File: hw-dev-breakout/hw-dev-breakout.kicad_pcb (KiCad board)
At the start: 4 copper layers, 176 parts, among them J101 CN7, J102 CN10, J201 WAGO 250-220, J202 Conn_01x16, J301 WAGO 250-220, J302 Conn_01x20, Q301 2N7002, Q302 2N7002, Q303 2N7002, Q304 2N7002, Q305 2N7002, Q306 2N7002, Q307 2N7002, Q308 HL 20N04, Q309 HL 20N04, Q310 2N7002, Q311 Q_PMOS_HL_4485, SW101 SW_Push, U101 TCAN332, U102 TCAN332, U103 TCAN332, U201 CM1293A-04SO, U202 CM1293A-04SO, U203 CM1293A-04SO, U204 CM1293A-04SO

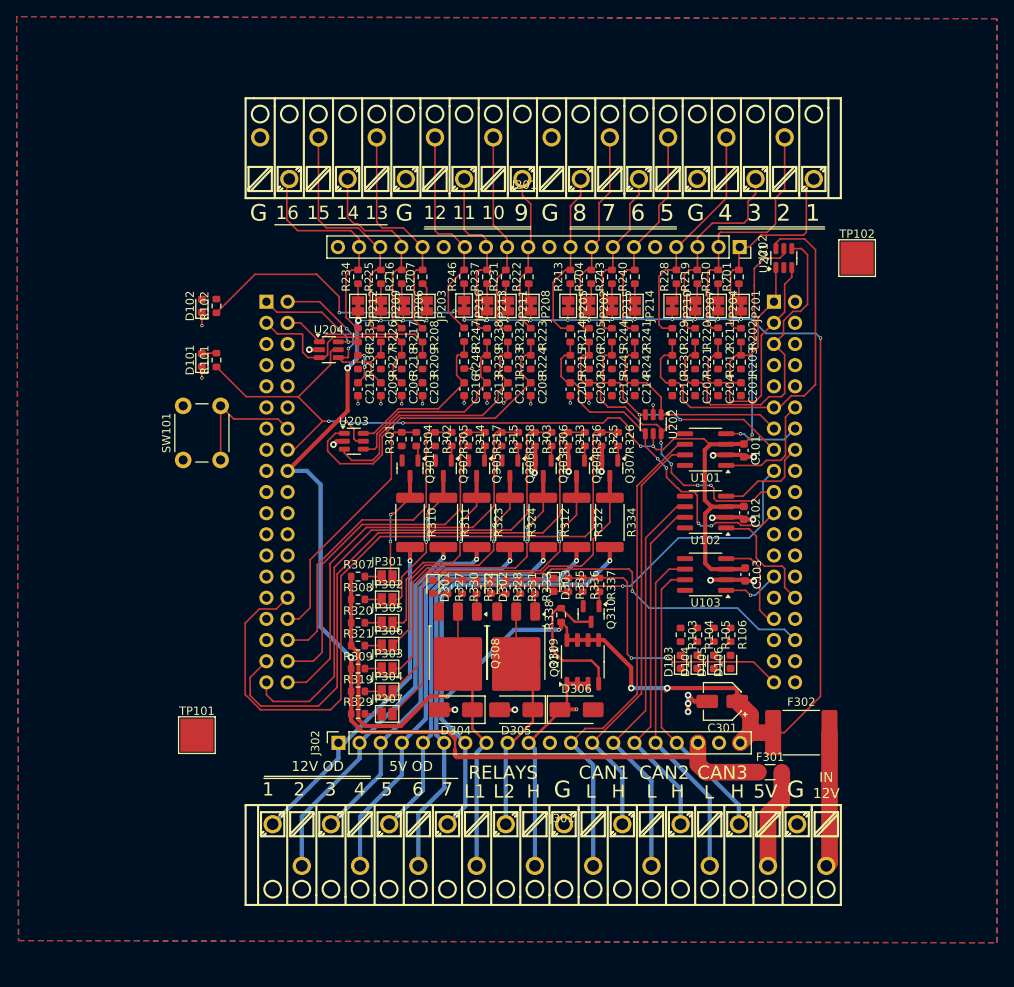
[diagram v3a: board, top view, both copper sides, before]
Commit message: pcb: Routed, using jlc 4 layer specs
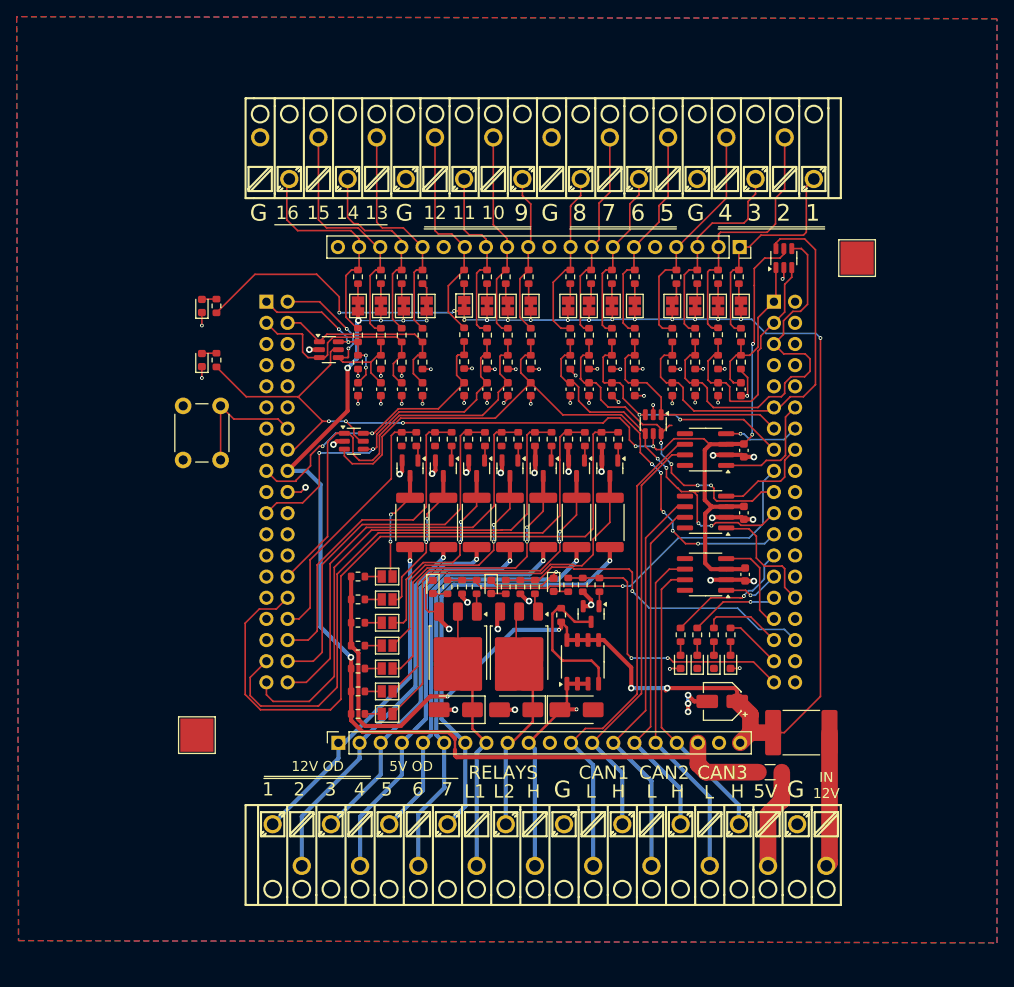
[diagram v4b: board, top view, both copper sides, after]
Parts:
- moved Q309 0.35 mm to (135.1, 104.5)
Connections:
- J102 pad 18: /LED4 -> unconnected-(J102-Pin_18-Pad18)
- J102 pad 2: /LED1 -> unconnected-(J102-Pin_2-Pad2)
- J102 pad 25: unconnected-(J102-Pin_25-Pad25) -> /LED1
- J102 pad 29: unconnected-(J102-Pin_29-Pad29) -> /LED2
- J102 pad 33: unconnected-(J102-Pin_33-Pad33) -> /LED3
- J102 pad 35: unconnected-(J102-Pin_35-Pad35) -> /LED4
- J102 pad 4: /LED2 -> unconnected-(J102-Pin_4-Pad4)
- J102 pad 6: /LED3 -> unconnected-(J102-Pin_6-Pad6)
- U203 pad 1: /IN9 -> /IN10
- U203 pad 3: /IN10 -> /IN9
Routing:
- net GND: track 50.4 -> 110.7 mm, vias 30 -> 64
- net /IN9: track 40.2 -> 77.4 mm, vias 0 -> 5
- net /IN10: track 32.4 -> 54.6 mm
- net /IN11: track 25.3 -> 43.6 mm, vias 0 -> 2
- net /IN12: track 20.8 -> 37.2 mm, vias 0 -> 2
- net /LED1: track 0.00 -> 15.9 mm, vias 0 -> 1
- net /LED2: track 0.00 -> 10.7 mm, vias 0 -> 1
- net /LED3: track 0.00 -> 9.51 mm
- net /LED4: track 0.00 -> 6.86 mm
- net /IN3: track 41.6 -> 46.9 mm
- net /IN13: track 19.5 -> 24.1 mm
- net Net-(D102-A): track 0.00 -> 1.77 mm
- net Net-(D106-A): track 0.00 -> 1.64 mm
- net Net-(D105-A): track 0.00 -> 1.64 mm
- net Net-(D104-A): track 0.00 -> 1.64 mm
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
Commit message: pcb: Routed for 2 layer, fixed P-fet error
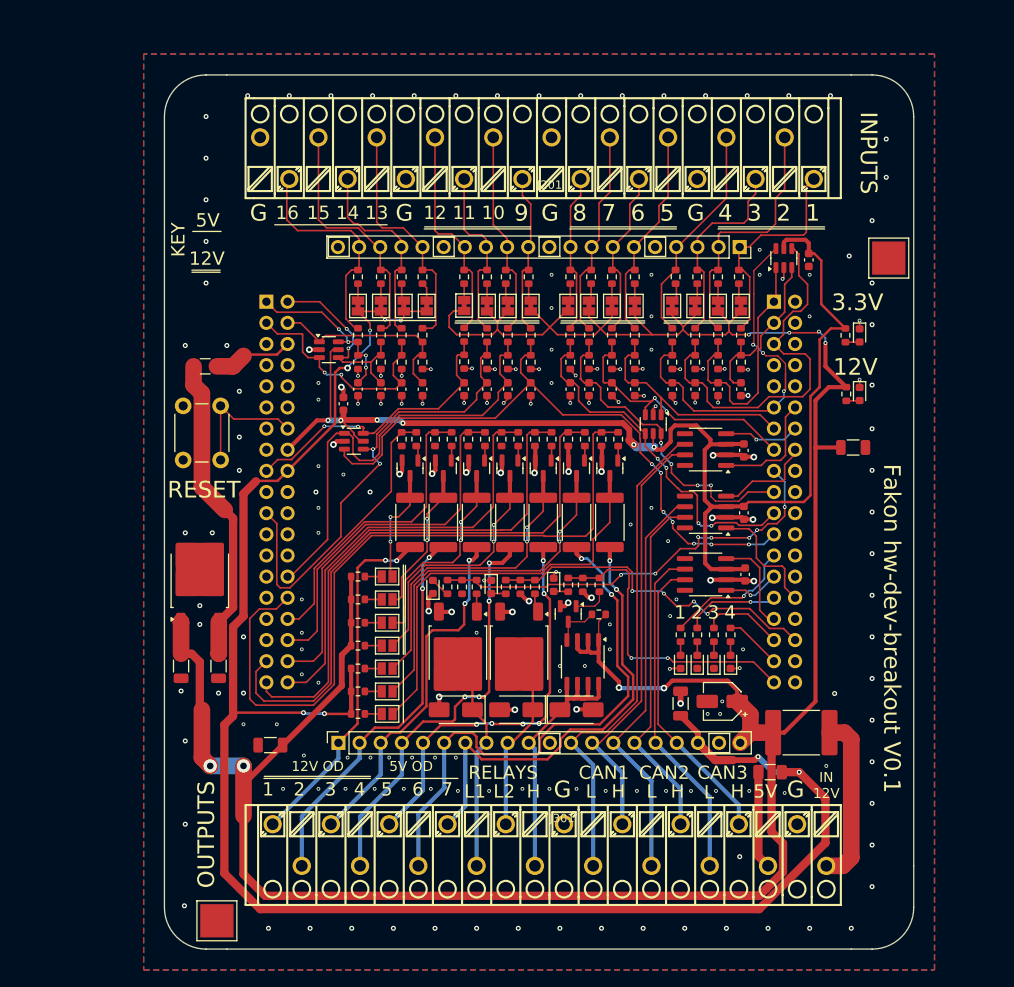
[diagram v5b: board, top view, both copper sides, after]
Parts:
- added C104: 1uF 50V, Capacitor_SMD:C_1206_3216Metric, F.Cu at (154.5, 110.5)
- added C105: 1uF 50V, Capacitor_SMD:C_1206_3216Metric, F.Cu at (175.2, 79.8)
- added C106: 1uF 50V, Capacitor_SMD:C_1206_3216Metric, F.Cu at (105.2, 115.5)
- added C107: 1uF 50V, Capacitor_SMD:C_1206_3216Metric, F.Cu at (99.0, 106.0)
- added C108: 1uF 50V, Capacitor_SMD:C_1206_3216Metric, F.Cu at (94.5, 106.0)
- added C217: 100nF, Capacitor_SMD:C_0603_1608Metric, F.Cu at (114.0, 74.5)
- added C218: 100nF, Capacitor_SMD:C_0603_1608Metric, F.Cu at (169.9, 57.2)
- added F101: 12H1100C 1A, Fuse:Fuse_1206_3216Metric, F.Cu at (97.4, 70.0)
- added U104: L7805, Package_TO_SOT_SMD:TO-252-2, F.Cu at (96.8, 95.7)
- J201, J301: footprint hw-dev-breakout:CONN-TH_250-220 -> hw-dev-breakout:WAGO 250-22
- Q308, Q309: footprint Package_TO_SOT_SMD:TO-252-3_TabPin2 -> Package_TO_SOT_SMD:TO-252-2
- TP101, TP102: footprint TestPoint:TestPoint_Pad_4.0x4.0mm -> hw-dev-breakout:TestPoint_Pad_4.0x4.0mm
- moved D102 79.7 mm to (176.0, 73.3), turned to -90 degrees
- moved D101 79.1 mm to (176.0, 66.3), turned to -90 degrees
- moved R102 76.4 mm to (174.4, 73.3), turned to -90 degrees
- moved R101 75.6 mm to (174.3, 66.3), turned to -90 degrees
- moved TP101 22.4 mm to (98.8, 136.6)
- moved R338 4.53 mm to (144.7, 99.8), turned to 180 degrees
- moved TP102 3.80 mm to (179.5, 57.0)
- moved Q310 2.75 mm to (141.0, 99.8)
- moved R228 0.10 mm to (153.9, 59.2)
- turned D301 to 90 degrees
- turned F301 to 180 degrees
- turned Q311 to -90 degrees
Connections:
- Q311 pad 1: /Outputs/12V_COIL_H -> +12V
- Q311 pad 2: /Outputs/12V_COIL_H -> +12V
- Q311 pad 3: /Outputs/12V_COIL_H -> +12V
- Q311 pad 5: +12V -> /Outputs/12V_COIL_H
- Q311 pad 6: +12V -> /Outputs/12V_COIL_H
- Q311 pad 7: +12V -> /Outputs/12V_COIL_H
- Q311 pad 8: +12V -> /Outputs/12V_COIL_H
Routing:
- net +12V: track 226.7 -> 395.0 mm, vias 19 -> 8
- net +5V: track 126.7 -> 217.2 mm, vias 6 -> 8
- net +3.3V: track 152.1 -> 192.7 mm, vias 7 -> 6
- net /5V_REGOUT: track 0.00 -> 37.2 mm
- net GND: track 110.7 -> 91.1 mm, vias 64 -> 205
- net /IN11: track 43.6 -> 57.6 mm
- net Net-(Q310-D): track 18.4 -> 5.53 mm
- net /Outputs/5V_OUT6: track 54.5 -> 65.2 mm, vias 1 -> 2
- net /E5V: track 0.00 -> 9.60 mm
- net /Outputs/12V_COIL_L2: track 25.7 -> 19.4 mm
- net /Outputs/12V_COIL_L1: track 32.4 -> 26.1 mm
- net /Outputs/12V_COIL_H: track 28.6 -> 33.9 mm, vias 1 -> 0
- net /IN4: track 50.2 -> 45.7 mm, vias 0 -> 3
- net /Outputs/12V_IN: track 16.2 -> 20.6 mm
- net /COIL_L1: track 48.6 -> 51.3 mm, vias 1 -> 7
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- removed copper zone on In1.Cu, net GND
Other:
- board outline added: 90 x 105 mm
- copper layers 4 -> 2
- board text added: "12V"
- board text added: "3.3V"
- board text added: "Fakon hw-dev-breakout V0.1"
- board text added: "INPUTS"
- board text added: "KEY"
- board text added: "OUTPUTS"
- board text added: "RESET"

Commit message: Add reverse polarity protection for 12V In
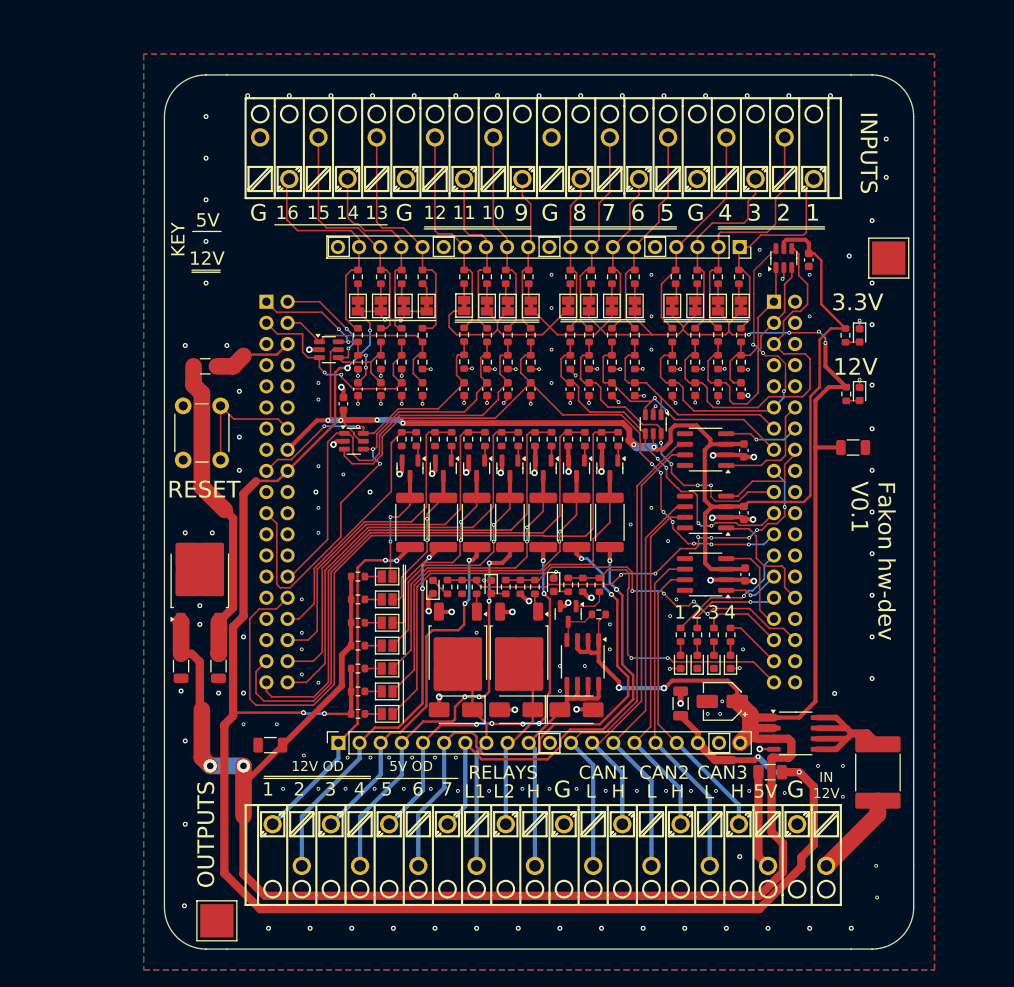
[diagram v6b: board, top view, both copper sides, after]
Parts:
- added Q312: Q_PMOS_HL_4485, Package_SO:SOP-8_3.9x4.9mm_P1.27mm, F.Cu at (168.3, 114.1)
- moved F302 10.4 mm to (178.2, 118.8), turned to -90 degrees
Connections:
- F302 pad 1: +12V -> Net-(F302-Pad1)
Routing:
- net Net-(F302-Pad1): track 0.00 -> 22.3 mm
- net /Outputs/12V_IN: track 20.6 -> 10.4 mm
- net +12V: track 395.0 -> 403.8 mm
- net GND: track 91.1 -> 92.8 mm
- net +5V: track 217.2 -> 216.0 mm
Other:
- board text added: "Fakon hw-dev V0.1"
- board text removed: "Fakon hw-dev-breakout V0.1"

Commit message: Final cleanups for initial fab run
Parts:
- D101, D102: value RED -> LED_RED
- D103, D104, D105, D106: value GREEN -> LED_GREEN; footprint LED_SMD:LED_0603_1608Metric -> LED_SMD:LED_0805_2012Metric
- D301, D302, D303: value ORANGE -> LED_YELLOW
- Q308, Q309: value HL 20N04 -> HD60N03
- U101, U102, U103: value TCAN332 -> SN65HVD232DR
- moved TP101 4.10 mm to (98.8, 132.5)
- moved D103 0.40 mm to (154.1, 105.5)
- moved R103 0.40 mm to (154.1, 102.2)
- moved D106 0.30 mm to (160.8, 105.5)
- moved R106 0.30 mm to (160.8, 102.2)
- moved D104 0.20 mm to (156.3, 105.5)
- moved R104 0.20 mm to (156.3, 102.2)
- moved D105 0.10 mm to (158.6, 105.5)
- moved R105 0.10 mm to (158.6, 102.2)
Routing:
- net +12V: track 403.8 -> 343.4 mm
- net GND: track 92.8 -> 97.0 mm, vias 205 -> 206
- net +5V: track 216.0 -> 214.5 mm
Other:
- board size 90 x 105 mm -> 90 x 100 mm
